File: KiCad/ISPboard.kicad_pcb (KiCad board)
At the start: 2 copper layers, 80 x 50 mm, 25 parts, among them IC1 ATMEGA328-P, P1 CONN_01X02, P2 ISP, P3 PB, P4 PC, P5 PD, P6 LED OUT, P7 BUTTON OUT, P8 CONN_01X02, SW1 PUSH 1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

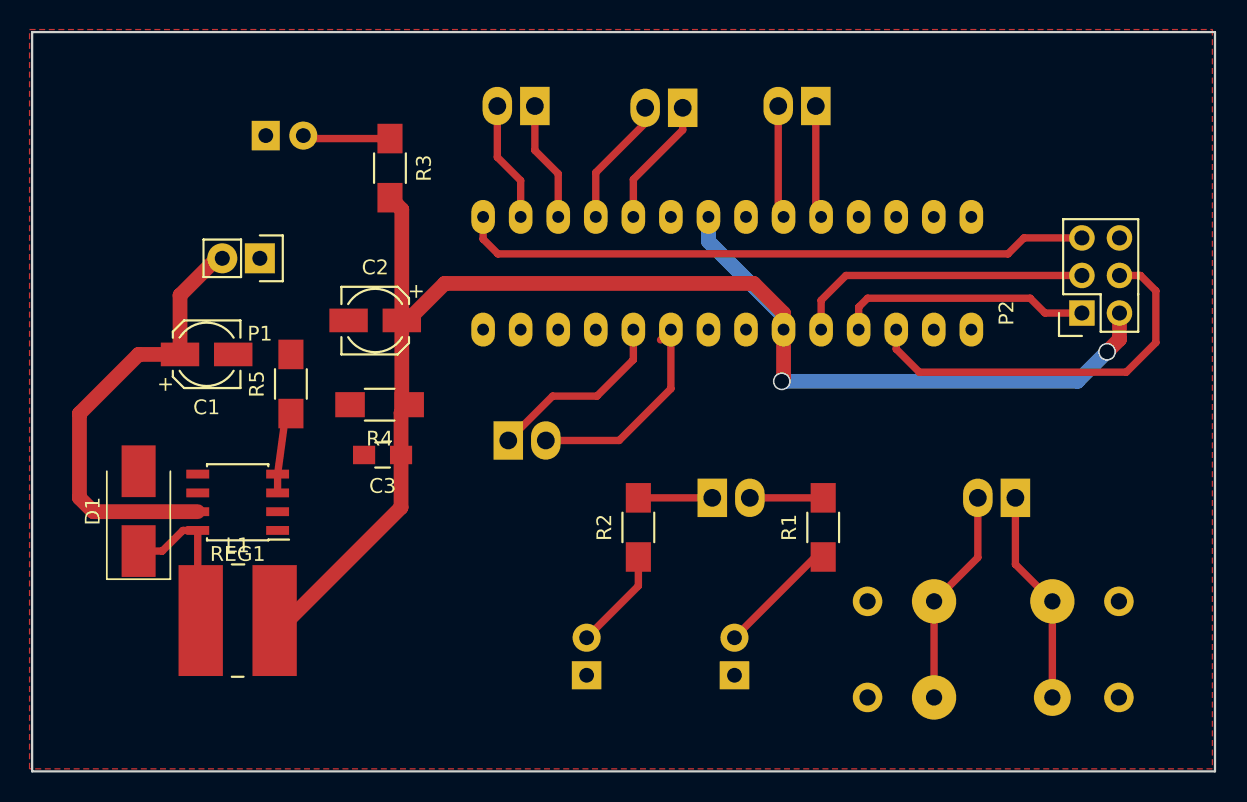
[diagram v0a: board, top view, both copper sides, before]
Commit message: Changed layout to have filled zones for input regulator
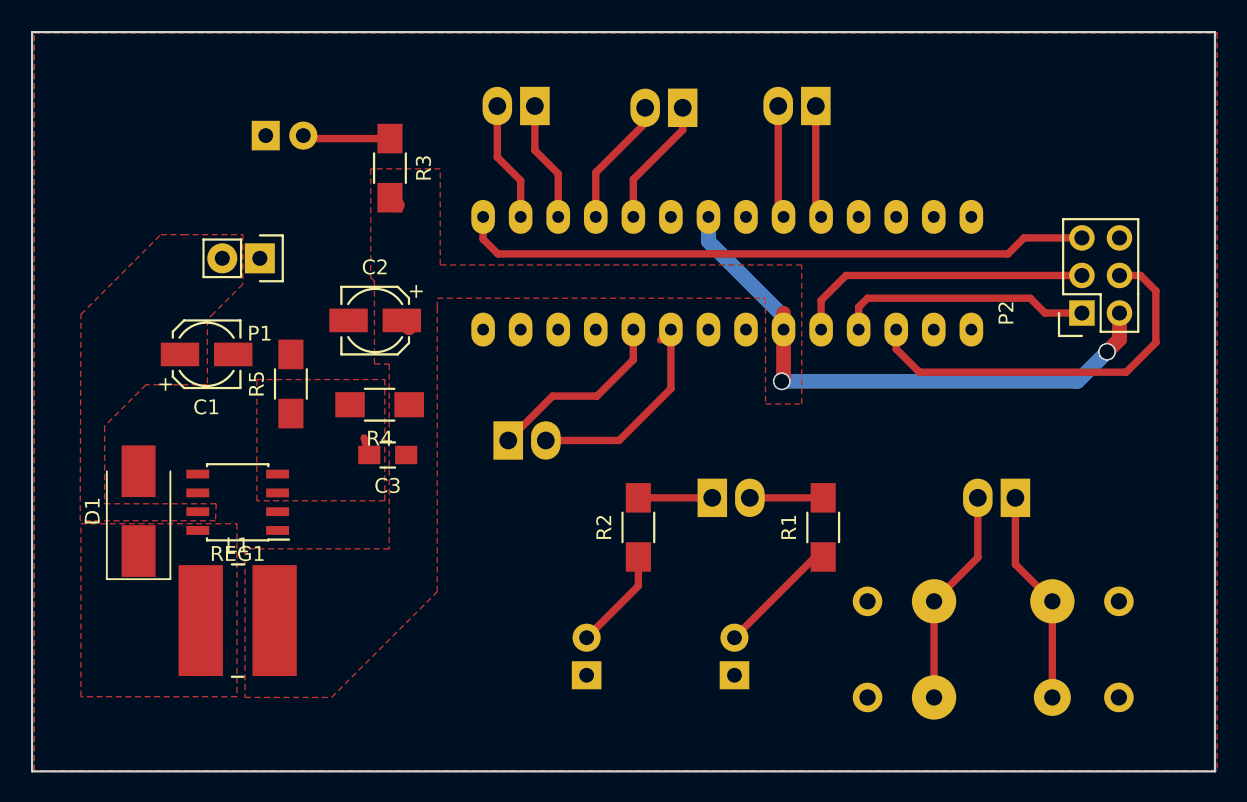
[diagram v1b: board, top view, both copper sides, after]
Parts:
- moved C3 0.35 mm to (129.1, 118.6)
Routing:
- net VDD: track 103.5 -> 44.7 mm
- net VCC: track 30.7 -> 1.43 mm
- net Net-(D1-Pad1): track 11.7 -> 1.27 mm
- net Net-(C3-Pad2): track 5.71 -> 1.20 mm
- added copper zone on F.Cu, net Net-(C3-Pad2)
- added copper zone on F.Cu, net Net-(D1-Pad1)
- added copper zone on F.Cu, net VCC
- added copper zone on F.Cu, net VDD
